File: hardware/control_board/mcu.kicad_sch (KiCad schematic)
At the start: 26 parts, among them IC1 24LC512, IC10 ATMEGA644p, J1 Conn_01x08, J2 Conn_01x06, Q1 20MHz, U1 AVR ISP, X1 MIDI, X2 MIDI

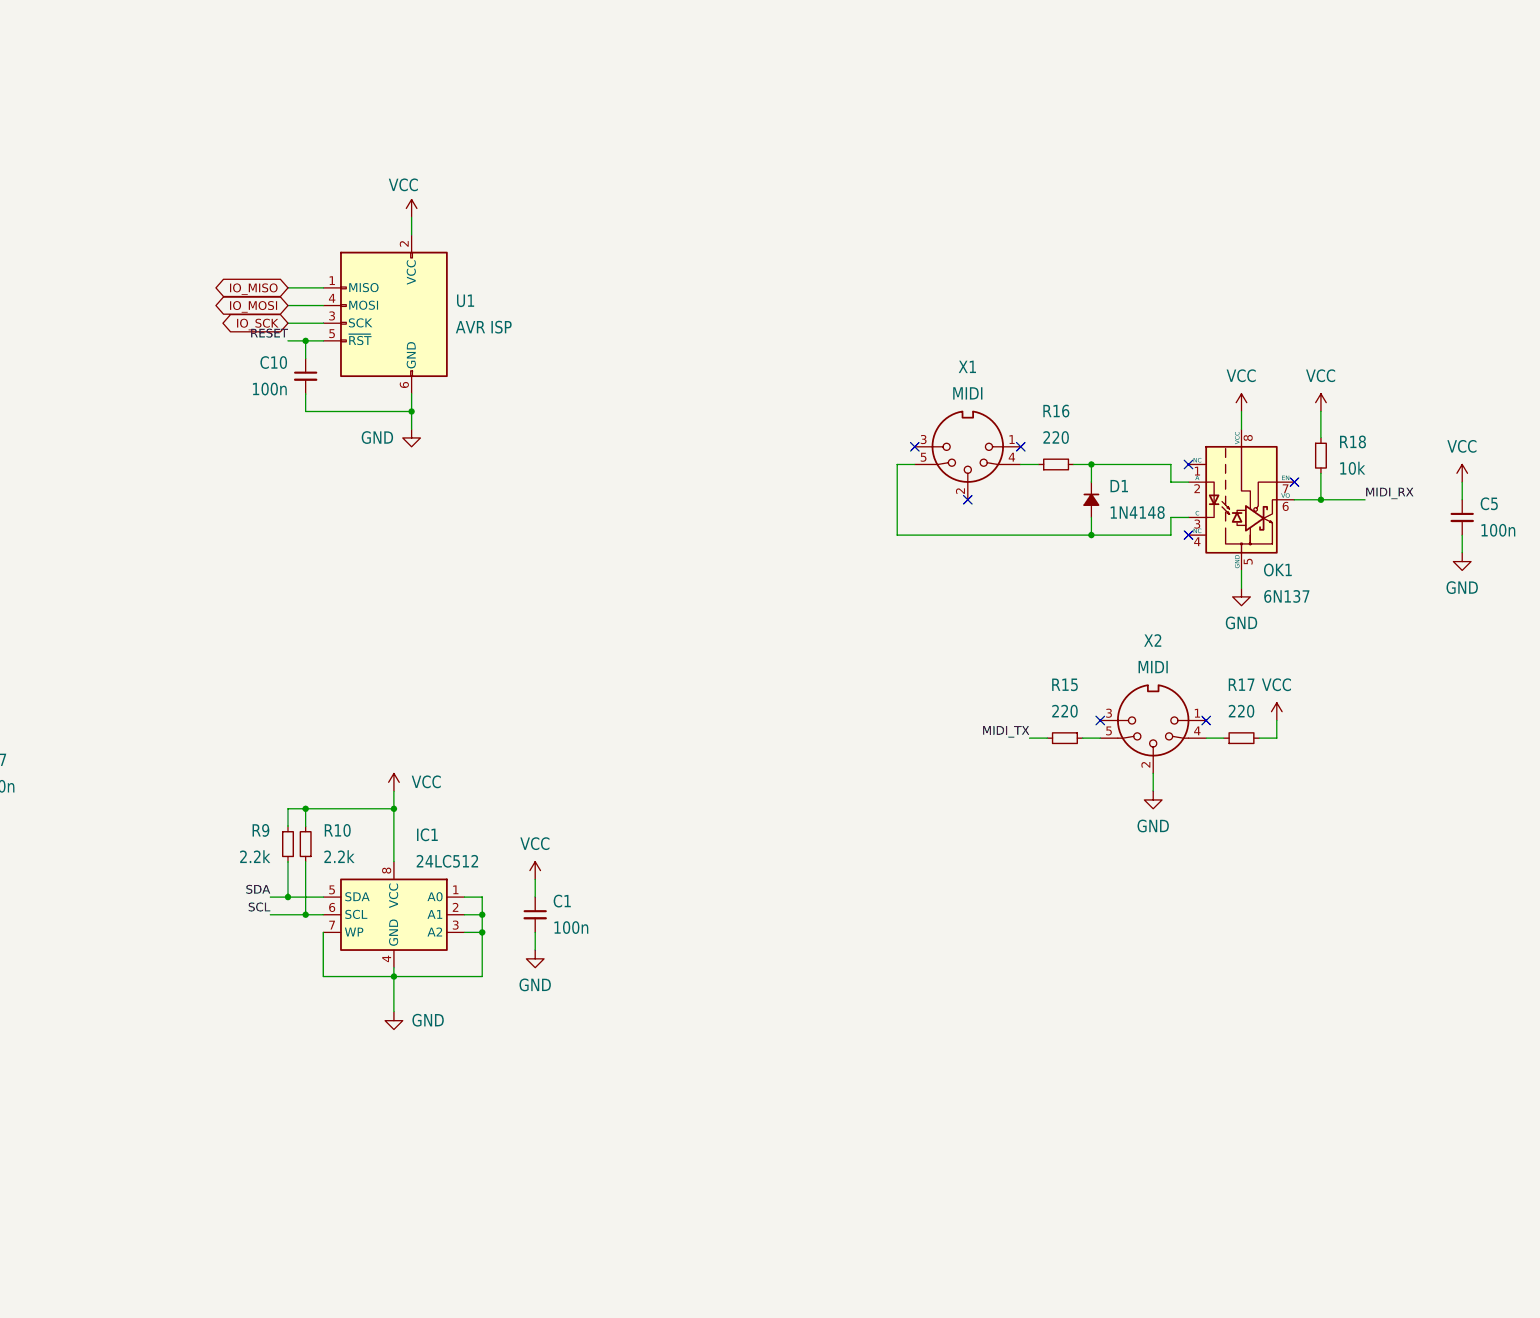
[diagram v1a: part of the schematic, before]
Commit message: move midi components to daughterboard
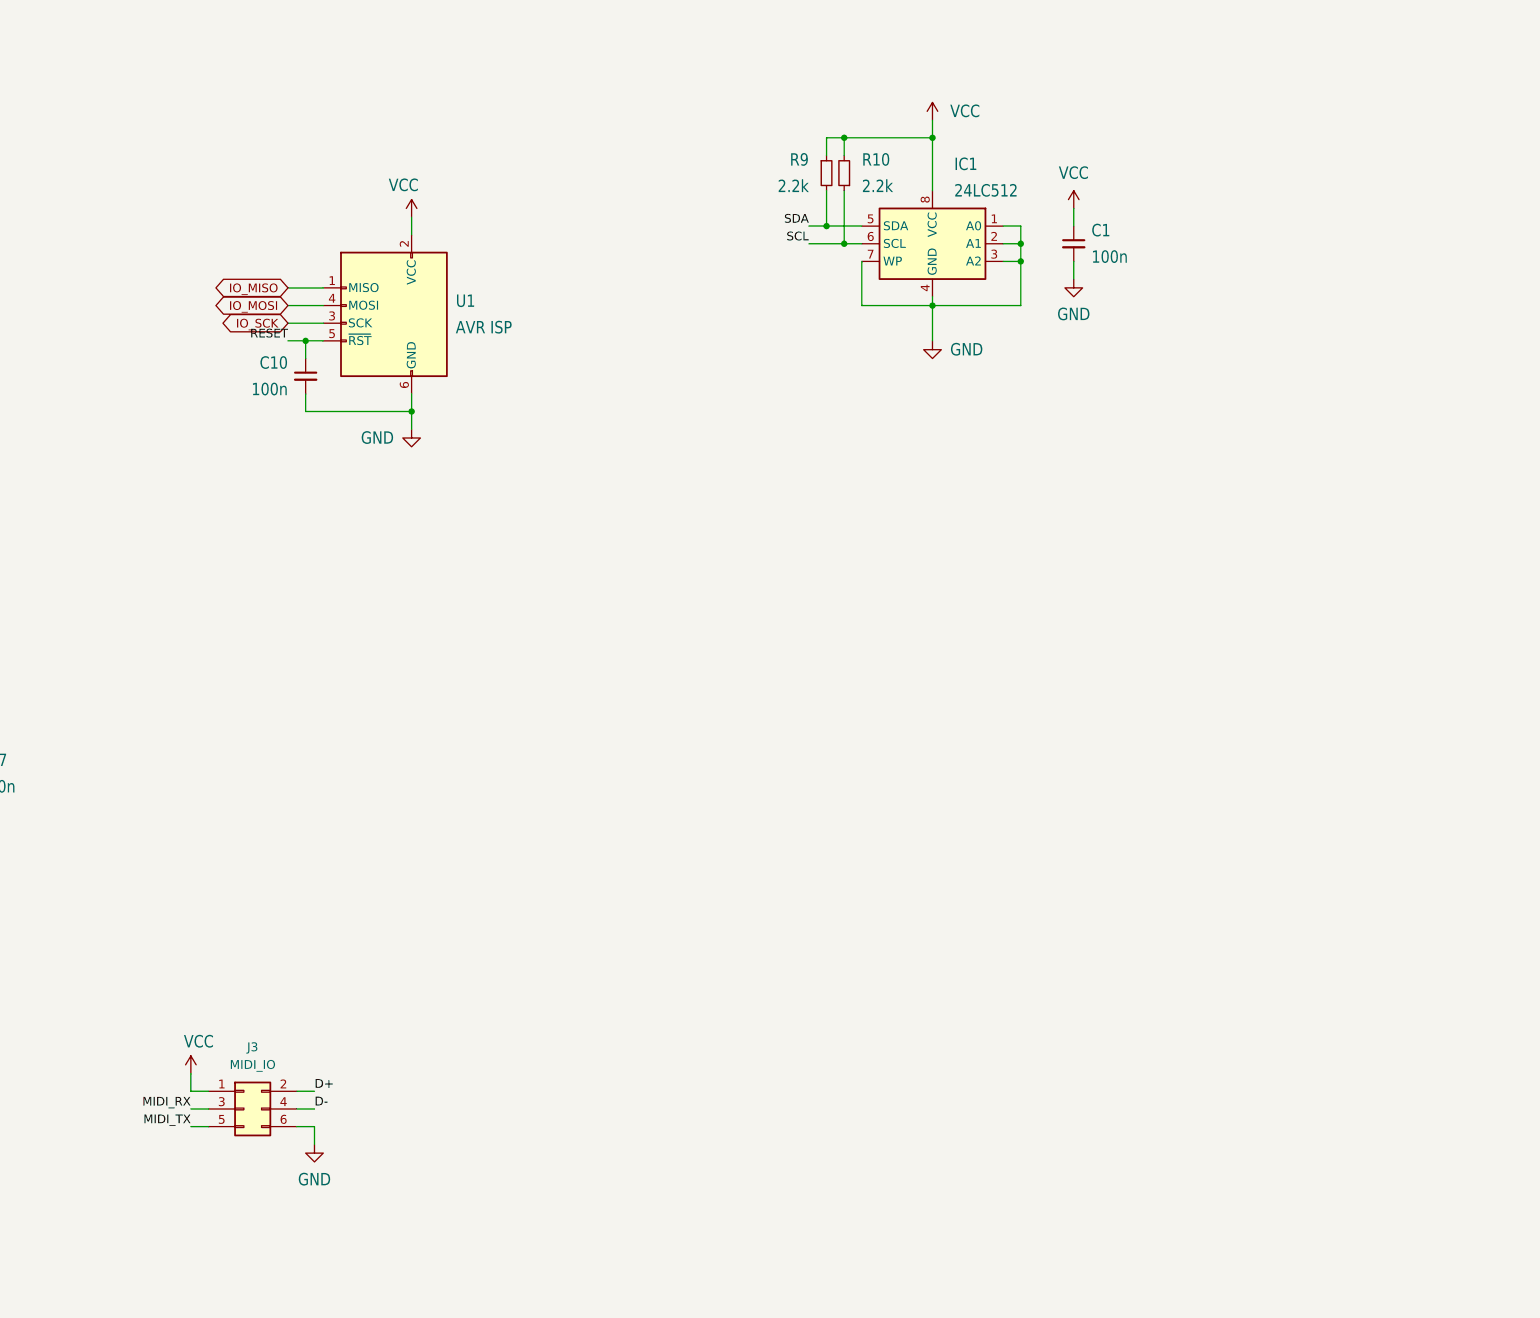
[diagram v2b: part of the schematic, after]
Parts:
- removed C5: 100n, shruthi_control_board_xt_v03:C025-024X044, symbol Device:C_Small
- removed D1: 1N4148, Diode_THT:D_DO-35_SOD27_P7.62mm_Horizontal, symbol Device:D_Small_Filled
- removed OK1: 6N137, Package_DIP:DIP-8_W7.62mm_Socket_LongPads, symbol Isolator:6N137
- removed R15, R16, R17: 220, Resistor_THT:R_Axial_DIN0204_L3.6mm_D1.6mm_P7.62mm_Horizontal, symbol Device:R_Small
- removed R18: 10k, Resistor_THT:R_Axial_DIN0204_L3.6mm_D1.6mm_P7.62mm_Horizontal, symbol Device:R_Small
- removed X1, X2: MIDI, shruthi_control_board_xt_v03:MAB5SH, symbol Connector:DIN-5_180degree
- added J3: MIDI_IO, Connector_PinHeader_2.54mm:PinHeader_2x03_P2.54mm_Vertical, symbol Connector_Generic:Conn_02x03_Odd_Even
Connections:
- net GND: now also J3.6 (Pin_6)
- net MIDI_RX: now also J3.3 (Pin_3)
- net MIDI_TX: now also J3.5 (Pin_5)
- net VCC: now also J3.1 (Pin_1)
- new net D+: J3.2 (Pin_2)
- new net D-: J3.4 (Pin_4)
- no-connect marks 8 -> 0
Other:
- moved on the sheet: C1, IC1, R10, R9
